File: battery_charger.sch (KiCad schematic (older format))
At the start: 23 parts, among them U48 BQ24190

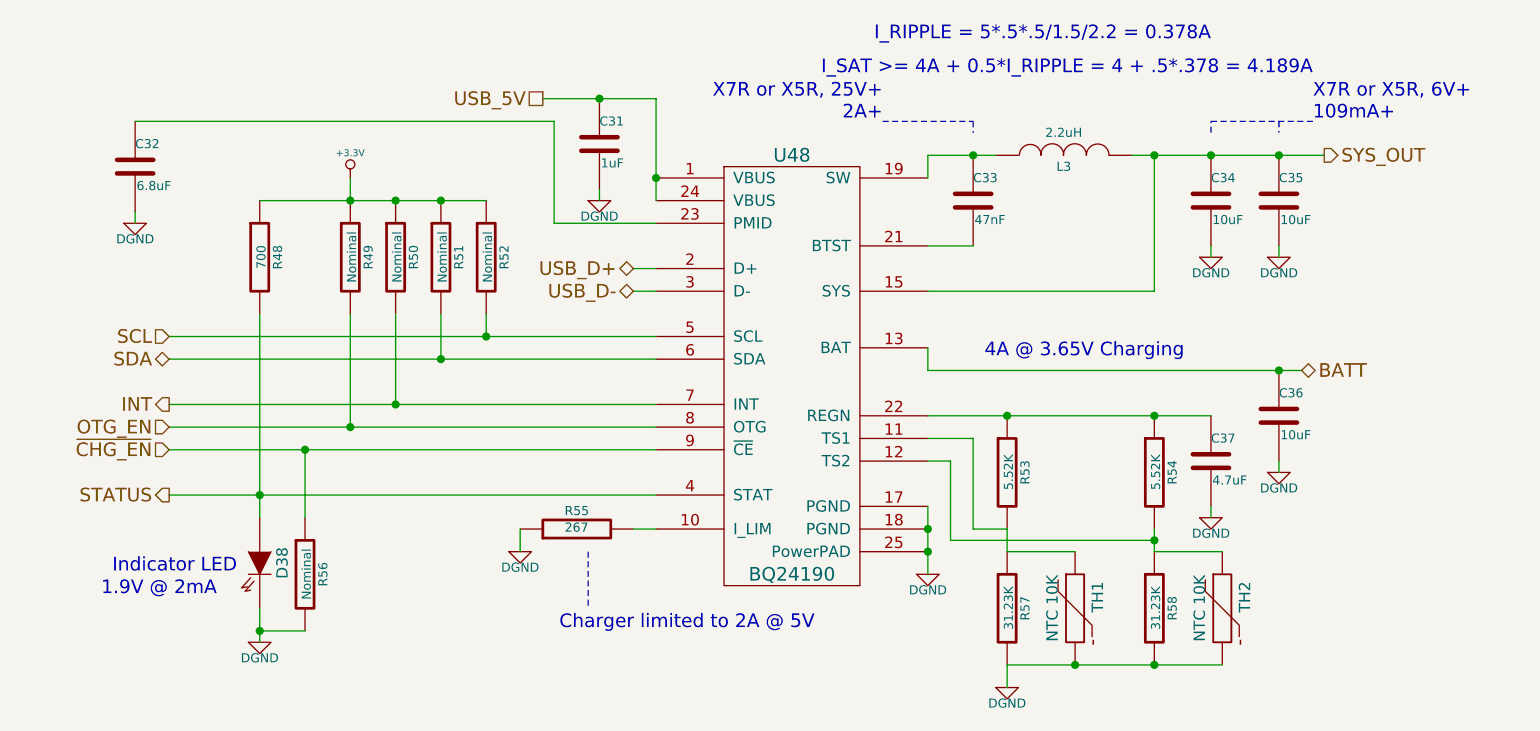
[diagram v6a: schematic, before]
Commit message: found error in schematic, charger stat LED
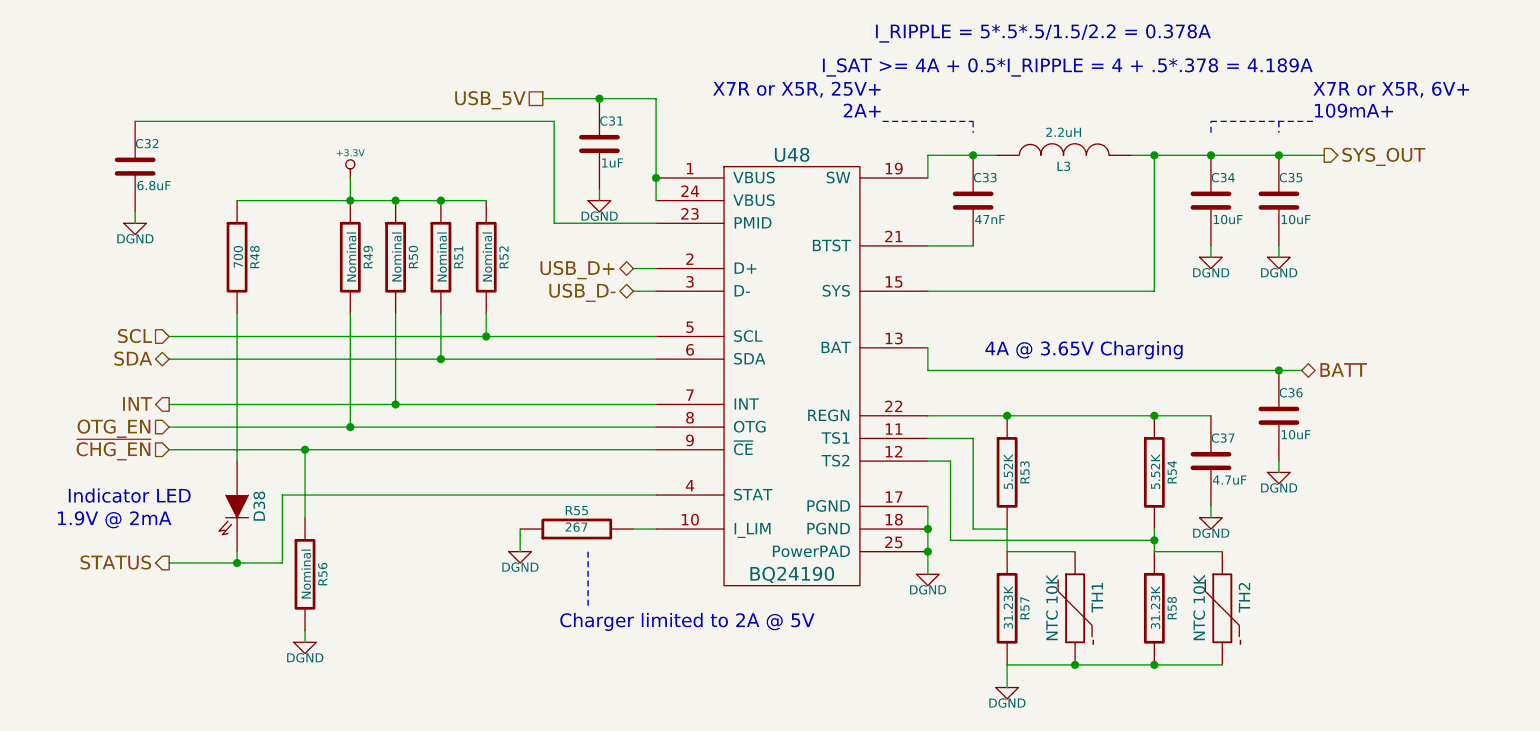
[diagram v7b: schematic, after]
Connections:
- net DGND: no longer D38.2 (Cathode)
- net STATUS: now also D38.2 (Cathode); no longer D38.1 (Anode), R48.2
- new net: D38.1 (Anode), R48.2
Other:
- moved on the sheet: D38, R48
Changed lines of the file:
@@
 $Descr A4 11693 8268
 encoding utf-8
-Sheet 16 16
+Sheet 15 16
 Title ""
-Date "22 feb 2014"
+Date "27 feb 2014"
 Rev ""
 Comp ""
@@
 	0    -1   -1   0
 $EndComp
-Text HLabel 2050 3150 0    60   Output ~ 0
+Text HLabel 2050 3450 0    60   Output ~ 0
 STATUS
 $Comp
@@
 $EndComp
 Wire Wire Line
-	2450 1850 3450 1850
+	2350 1850 3450 1850
 Connection ~ 3250 1850
 $Comp
@@
 	2850 1750 2850 1850
 Connection ~ 3050 1850
-Wire Wire Line
-	2050 3150 4200 3150
 $Comp
 L C C36
@@
 Text Notes 6650 1150 2    60   ~ 0
 I_RIPPLE = 5*.5*.5/1.5/2.2 = 0.378A
-Text Notes 2350 3500 2    60   ~ 0
+Text Notes 2150 3200 2    60   ~ 0
 Indicator LED
 $Comp
 L LED_GENERIC_SMD D38
 U 1 1 52B37BFF
-P 2450 3450
-F 0 "D38" H 2450 3550 50  0000 C CNN
-F 1 "LED_GENERIC_SMD" H 2450 3300 50  0001 C CNN
-F 2 "~" H 2450 3450 60  0000 C CNN
-F 3 "~" H 2450 3450 60  0000 C CNN
-	1    2450 3450
+P 2350 3200
+F 0 "D38" H 2350 3300 50  0000 C CNN
+F 1 "LED_GENERIC_SMD" H 2350 3050 50  0001 C CNN
+F 2 "~" H 2350 3200 60  0000 C CNN
+F 3 "~" H 2350 3200 60  0000 C CNN
+	1    2350 3200
 	0    1    1    0
 $EndComp
-Text Notes 1750 3600 0    60   ~ 0
+Text Notes 1550 3300 0    60   ~ 0
 1.9V @ 2mA
 $Comp
 L DGND #PWR0108
 U 1 1 52B37C0F
-P 2450 3800
-F 0 "#PWR0108" H 2450 3800 40  0001 C CNN
-F 1 "DGND" H 2450 3730 40  0000 C CNN
-F 2 "" H 2450 3800 60  0000 C CNN
-F 3 "" H 2450 3800 60  0000 C CNN
-	1    2450 3800
-	1    0    0    -1
-$EndComp
-Wire Wire Line
-	2450 3800 2450 3650
+P 2650 3800
+F 0 "#PWR0108" H 2650 3800 40  0001 C CNN
+F 1 "DGND" H 2650 3730 40  0000 C CNN
+F 2 "" H 2650 3800 60  0000 C CNN
+F 3 "" H 2650 3800 60  0000 C CNN
+	1    2650 3800
+	1    0    0    -1
+$EndComp
 Wire Notes Line
 	3900 3400 3900 3650
@@
 L R R48
 U 1 1 52B3BA8E
-P 2450 2100
-F 0 "R48" V 2530 2100 40  0000 C CNN
-F 1 "700" V 2457 2101 40  0000 C CNN
-F 2 "~" V 2380 2100 30  0000 C CNN
-F 3 "~" H 2450 2100 30  0000 C CNN
-	1    2450 2100
-	1    0    0    -1
-$EndComp
-Wire Wire Line
-	2450 2350 2450 3250
-Connection ~ 2450 3150
+P 2350 2100
+F 0 "R48" V 2430 2100 40  0000 C CNN
+F 1 "700" V 2357 2101 40  0000 C CNN
+F 2 "~" V 2280 2100 30  0000 C CNN
+F 3 "~" H 2350 2100 30  0000 C CNN
+	1    2350 2100
+	1    0    0    -1
+$EndComp
 Wire Wire Line
 	2650 2950 2650 3250
@@
 	1    0    0    -1
 $EndComp
-Wire Wire Line
-	2450 3750 2650 3750
-Connection ~ 2450 3750
 Connection ~ 6050 3900
 Connection ~ 6400 3900
@@
 Wire Wire Line
 	5400 2500 5400 2600
+Wire Wire Line
+	2650 3750 2650 3800
+Wire Wire Line
+	2550 3450 2550 3150
+Wire Wire Line
+	2550 3150 4200 3150
+Wire Wire Line
+	2350 2350 2350 3000
+Wire Wire Line
+	2050 3450 2550 3450
+Wire Wire Line
+	2350 3450 2350 3400
+Connection ~ 2350 3450
 $EndSCHEMATC
